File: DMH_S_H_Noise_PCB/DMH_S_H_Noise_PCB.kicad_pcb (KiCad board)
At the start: 2 copper layers, 48 x 120.8 mm, 82 parts, among them J0 Conn_01x01, J100 IDC_02x05, J200 IDC_02x05, J50 Conn_01x06, J60 Conn_01x06, J70 Conn_01x06, Q1 BC548, Q2 J113, Q3 BC548, SW1 SW_Push, SW2 SW_SPDT_321, U1 TL074, U2 TL074, U3 TL074

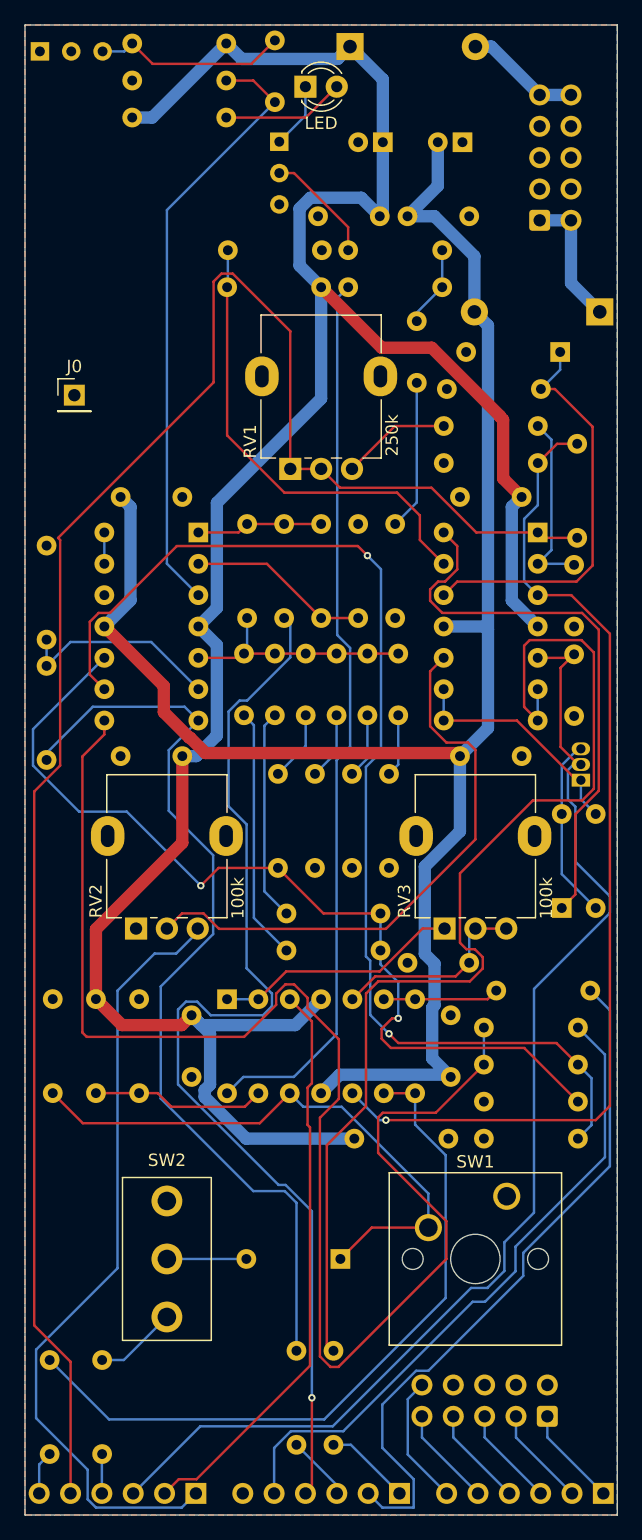
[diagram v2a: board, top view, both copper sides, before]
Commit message: Restarted positioning from scratch
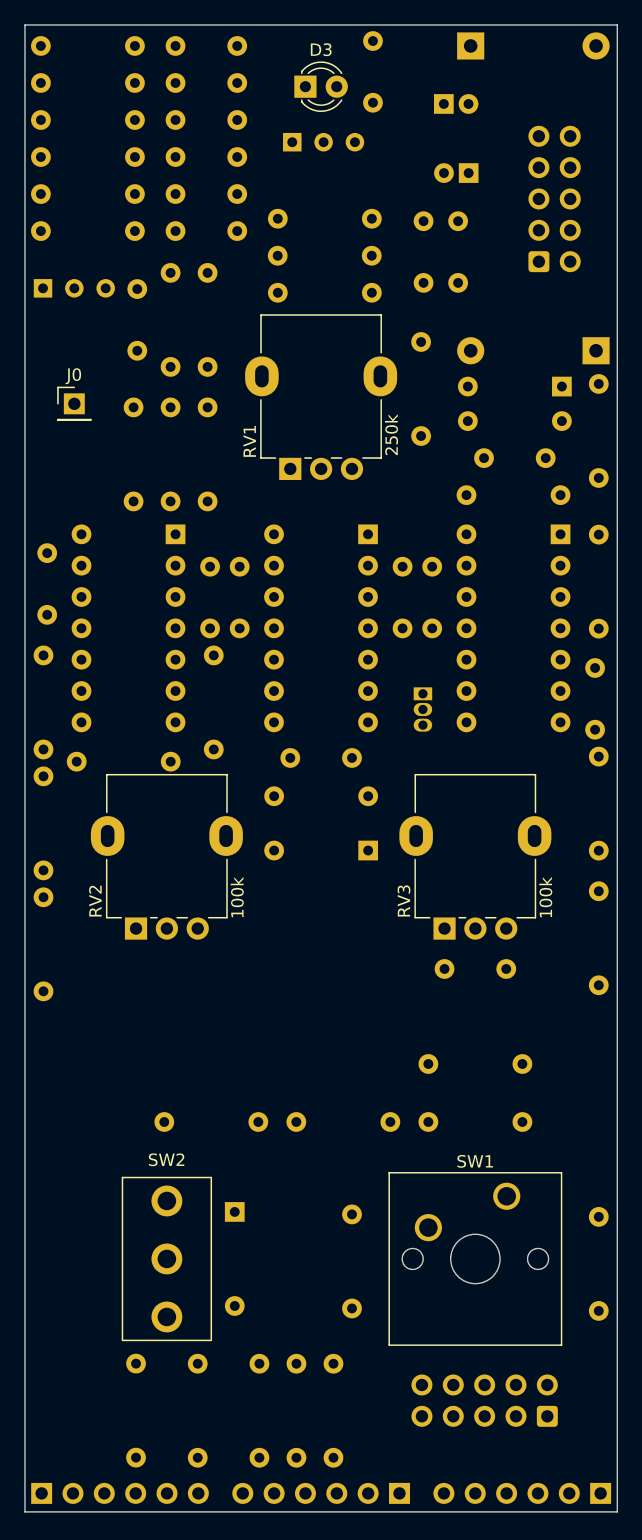
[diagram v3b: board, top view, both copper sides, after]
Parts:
- C10: value 1nF -> 100nF
- C11: value 100nF -> 2x1uF
- C12: value 1uF -> 1nF
- C13, C9: value 1uF -> 100nF
- C14: value 680pF -> 2x470nF
- C15: value 2.2nF -> 1uF
- C16: value 5.6nF -> 680pF
- C17: value 680pF -> 2.2nF
- C18: value 2.2nF -> 5.6nF
- C20: value 100nF -> 2.2nF
- C21: value 100nF -> 680pF
- D1: value LED -> SB140-; footprint LED_THT:LED_D3.0mm -> Diode_THT:D_DO-41_SOD81_P10.16mm_Horizontal; moved to B.Cu
- D2: value 1N4148 -> SB140+; footprint Diode_THT:D_DO-35_SOD27_P7.62mm_Horizontal -> Diode_THT:D_DO-41_SOD81_P10.16mm_Horizontal
- D3: value 1N4148 -> LED; footprint Diode_THT:D_DO-35_SOD27_P7.62mm_Horizontal -> LED_THT:LED_D3.0mm; moved to F.Cu
- D4: value SB140- -> 1N4148; footprint Diode_THT:D_DO-41_SOD81_P10.16mm_Horizontal -> Diode_THT:D_DO-35_SOD27_P7.62mm_Horizontal
- D5: value SB140+ -> 1N4148; footprint Diode_THT:D_DO-41_SOD81_P10.16mm_Horizontal -> Diode_THT:D_DO-35_SOD27_P7.62mm_Horizontal
- R1: value 100k -> 2x2k
- R11: value 1M -> 100k
- R12: value 1k -> 33k
- R13: value 1k -> 100k
- R14: value 100k -> 51k
- R15: value 100k -> 1M
- R16: value 270R -> 1k
- R17, R37: value 100k -> 1k
- R2, R6: value 2k -> 100k
- R20: value 4k7 -> 100k
- R21: value 47k -> 270R
- R22: value 470k -> 100k
- R23: value 22k -> 1k
- R25: value 1k -> 4k7
- R26: value 1M -> 47k
- R28: value 10k -> 22k
- R29: value 20k -> 100k
- R30: value 10k -> 1k
- R31: value 100K -> 1M
- R32: value 1k -> 470k
- R33: value 1k -> 10k
- R34: value 100k -> 20k
- R36: value 100k -> 100K
- R38: value 100k -> 2k
- R5: value 51k -> 100k
- R7: value 100k -> 10k
- R9: value 33k -> 100k
- moved R33 114.1 mm to (52.3, 44.2), turned to 0 degrees
- moved R25 105.2 mm to (59.9, 53.2), turned to 180 degrees
- moved R31 88.1 mm to (52.3, 50.2), turned to 0 degrees
- moved R32 88.1 mm to (52.3, 47.2), turned to 0 degrees
- moved R6 87.3 mm to (91.3, 131.4), turned to 180 degrees
- moved D4 78.7 mm to (68.0, 138.7), turned to -90 degrees
- moved D3 69.7 mm to (73.7, 47.5), turned to 0 degrees
- moved R23 69.3 mm to (73.0, 158.6)
- moved R18 68.4 mm to (65.0, 158.6)
- moved R5 67.4 mm to (91.3, 126.7), turned to 180 degrees
- moved R38 67.1 mm to (79.1, 58.2), turned to 180 degrees
- moved R26 64.4 mm to (59.9, 56.2)
- moved R17 63.6 mm to (77.5, 146.5), turned to 90 degrees
- moved R8 60.6 mm to (80.6, 131.4)
- moved C12 60.2 mm to (83.3, 58.4), turned to -90 degrees
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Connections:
- C10 pad 1: Net-(D2-A) -> GND
- C10 pad 2: Net-(C10-Pad2) -> -12V
- C11 pad 1: /Core Circuit/S&H -> GND
- C11 pad 2: GND -> Net-(U1A--)
- C12 pad 1: Net-(U2B-+) -> Net-(D5-A)
- C12 pad 2: GND -> Net-(C12-Pad2)
- C13 pad 1: Net-(Q3-E) -> /Core Circuit/S&H
- C13 pad 2: Net-(U3A-+) -> GND
- C14 pad 1: Net-(U3B-+) -> Net-(U2B-+)
- C14 pad 2: Net-(C14-Pad2) -> GND
- C15 pad 1: Net-(U3B-+) -> Net-(Q3-E)
- C15 pad 2: Net-(C15-Pad2) -> Net-(U3A-+)
- C20 pad 1: +12V -> Net-(U3B-+)
- C20 pad 2: GND -> Net-(C20-Pad2)
- C21 pad 1: GND -> Net-(U3B-+)
- C21 pad 2: -12V -> Net-(C21-Pad2)
- C9 pad 1: GND -> +12V
- C9 pad 2: Net-(U1A--) -> GND
- D1 pad 2: Net-(D1-A) -> -12V
- D2 pad 1: Net-(D2-K) -> +12V
- D4 pad 2: -12V -> Net-(D4-A)
- D5 pad 1: +12V -> Net-(D5-K)
- J100 pad 1a: Net-(D4-K) -> Net-(D1-K)
- J100 pad 1b: Net-(D4-K) -> Net-(D1-K)
- J100 pad 5a: Net-(D5-A) -> Net-(D2-A)
- J100 pad 5b: Net-(D5-A) -> Net-(D2-A)
- Q1 pad 1: Net-(D1-K) -> Net-(D3-K)
- Q2 pad 3: Net-(D3-A) -> Net-(D6-A)
- R1 pad 1: Net-(U1A-+) -> Net-(R1-Pad1)
- R1 pad 2: GND -> Net-(U1A--)
- R10 pad 1: +12V -> Net-(D5-A)
- R10 pad 2: Net-(U1D--) -> GND
- R11 pad 1: Net-(Q2-D) -> Net-(D5-K)
- R11 pad 2: Net-(D3-A) -> GND
- R12 pad 1: /Core Circuit/S&H Output -> Net-(U1D--)
- R12 pad 2: Net-(U1B--) -> GND
- R13 pad 1: /Core Circuit/Slew Output -> +12V
- R13 pad 2: Net-(U2B--) -> Net-(U1D--)
- R14 pad 1: +12V -> Net-(Q1-B)
- R14 pad 2: Net-(Q3-E) -> Net-(D5-A)
- R15 pad 1: Net-(U3A-+) -> Net-(Q2-D)
- R15 pad 2: GND -> Net-(D6-A)
- R16 pad 1: Net-(U3A--) -> /Core Circuit/S&H Output
- R16 pad 2: GND -> Net-(U1B--)
- R17 pad 1: Net-(R17-Pad1) -> /Core Circuit/Slew Output
- R17 pad 2: Net-(U3A--) -> Net-(U2B--)
- R18 pad 1: /Core Circuit/White -> /Core Circuit/Clock Output
- R18 pad 2: Net-(R17-Pad1) -> Net-(U2C--)
- R19 pad 1: Net-(U3B-+) -> +12V
- R19 pad 2: Net-(R17-Pad1) -> Net-(Q3-E)
- R2 pad 1: Net-(R2-Pad1) -> Net-(U1A-+)
- R2 pad 2: Net-(U1A--) -> GND
- R20 pad 1: Net-(C14-Pad2) -> Net-(U3A-+)
- R21 pad 1: Net-(C15-Pad2) -> Net-(U3A--)
- R22 pad 1: Net-(C16-Pad2) -> Net-(R22-Pad1)
- R22 pad 2: GND -> Net-(U3A--)
- R23 pad 1: Net-(U3B--) -> /Core Circuit/White
- R23 pad 2: GND -> Net-(R22-Pad1)
- R24 pad 1: Net-(U3B--) -> Net-(U3B-+)
- R24 pad 2: Net-(R24-Pad2) -> Net-(R22-Pad1)
- R25 pad 1: /Core Circuit/Pink -> Net-(C16-Pad2)
- R25 pad 2: Net-(R24-Pad2) -> GND
- R26 pad 1: Net-(U3C-+) -> Net-(C17-Pad2)
- R26 pad 2: Net-(C19-Pad2) -> GND
- R27 pad 1: Net-(U3C-+) -> Net-(C18-Pad2)
- R27 pad 2: Net-(C18-Pad2) -> GND
- R28 pad 1: Net-(U3C-+) -> Net-(U3B--)
- R28 pad 2: Net-(C17-Pad2) -> GND
- R29 pad 1: Net-(U3C-+) -> Net-(U3B--)
- R29 pad 2: GND -> Net-(R29-Pad2)
- R30 pad 1: Net-(U3C--) -> /Core Circuit/Pink
- R30 pad 2: GND -> Net-(R29-Pad2)
- R31 pad 1: Net-(U3C--) -> Net-(U3C-+)
- R31 pad 2: Net-(R31-Pad2) -> Net-(C19-Pad2)
- R32 pad 1: /Core Circuit/Blue -> Net-(U3C-+)
- R32 pad 2: Net-(R31-Pad2) -> Net-(C20-Pad2)
- R33 pad 1: /Core Circuit/Clock Output -> Net-(U3C-+)
- R33 pad 2: Net-(U2C--) -> Net-(C21-Pad2)
- R34 pad 1: GND -> Net-(U3C-+)
- R34 pad 2: Net-(D6-K) -> GND
- R35 pad 1: Net-(U2D--) -> Net-(U3C--)
- R36 pad 1: Net-(R36-Pad1) -> Net-(U3C--)
- R36 pad 2: Net-(C10-Pad2) -> Net-(R36-Pad2)
- R37 pad 1: Net-(R37-Pad1) -> /Core Circuit/Blue
- R37 pad 2: +12V -> Net-(R36-Pad2)
- R38 pad 2: Net-(U2D--) -> Net-(D3-A)
- R5 pad 1: Net-(Q1-B) -> GND
- R5 pad 2: Net-(C10-Pad2) -> Net-(D4-K)
- R6 pad 1: +12V -> Net-(R6-Pad1)
- R6 pad 2: Net-(D1-A) -> +12V
- R7 pad 1: Net-(D2-A) -> Net-(U2D--)
- R8 pad 1: Net-(D2-K) -> +12V
- R8 pad 2: GND -> Net-(U2D--)
- R9 pad 1: Net-(U1D--) -> Net-(R9-Pad1)
- R9 pad 2: GND -> Net-(C12-Pad2)
- RV1 pad 3: Net-(R2-Pad1) -> Net-(R1-Pad1)
- SW1 pad 1: Net-(R37-Pad1) -> Net-(R6-Pad1)
- SW1 pad 2: Net-(D6-K) -> Net-(D4-K)
- SW2 pad 2: Net-(D6-A) -> Net-(D4-A)
- U1 pad 12: Net-(D2-K) -> Net-(D5-K)
- U1 pad 14: Net-(D3-K) -> Net-(D6-K)
- U2 pad 12: Net-(D6-K) -> Net-(D4-K)
- U2 pad 14: Net-(R36-Pad1) -> Net-(R9-Pad1)
- U3 pad 1: Net-(R17-Pad1) -> Net-(R22-Pad1)
- U3 pad 7: Net-(R24-Pad2) -> Net-(R29-Pad2)
- U3 pad 8: Net-(R31-Pad2) -> Net-(R36-Pad2)
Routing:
- net +12V: track 197.2 -> 0.00 mm
- net /Core Circuit/Internal Clock: track 150.7 -> 0.00 mm
- net -12V: track 144.9 -> 0.00 mm
- net Net-(R31-Pad2): track 119.2 -> 0.00 mm
- net /Core Circuit/S&H: track 97.6 -> 0.00 mm
- net Net-(U3C--): track 95.1 -> 0.00 mm, vias 2 -> 0
- net Net-(U1B--): track 89.7 -> 0.00 mm
- net /Core Circuit/White: track 88.4 -> 0.00 mm, vias 1 -> 0
- net Net-(U1A-+): track 83.1 -> 0.00 mm, vias 1 -> 0
- net Net-(R24-Pad2): track 76.2 -> 0.00 mm
- net Net-(U3C-+): track 75.1 -> 0.00 mm, vias 2 -> 0
- net Net-(R36-Pad1): track 72.7 -> 0.00 mm
- net /Core Circuit/Input: track 64.0 -> 0.00 mm
- net Net-(U2C--): track 58.7 -> 0.00 mm
- net /Core Circuit/Slew Output: track 56.0 -> 0.00 mm
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- removed copper zone on B.Cu, net GND
- removed copper zone on F.Cu, net GND
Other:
- board size 48 x 120.8 mm -> 48 x 120.5 mm

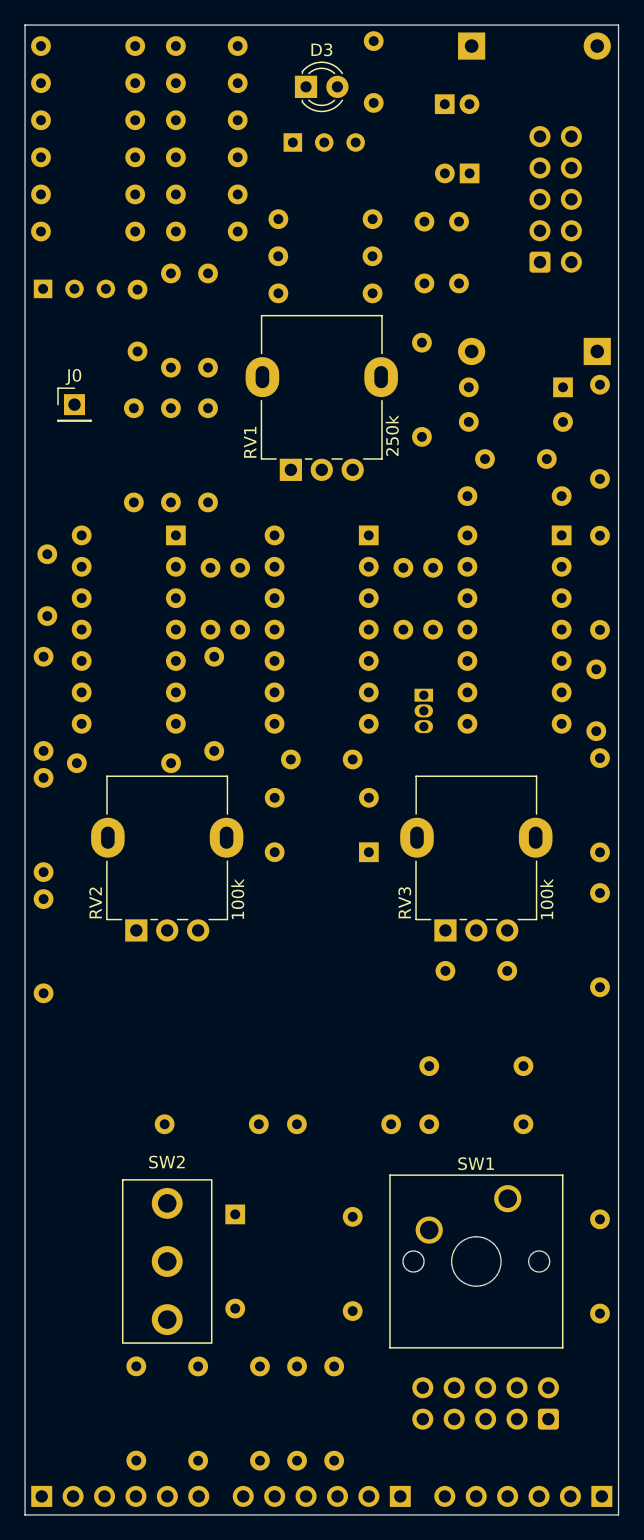
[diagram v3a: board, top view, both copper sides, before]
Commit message: Minor positioning corrections
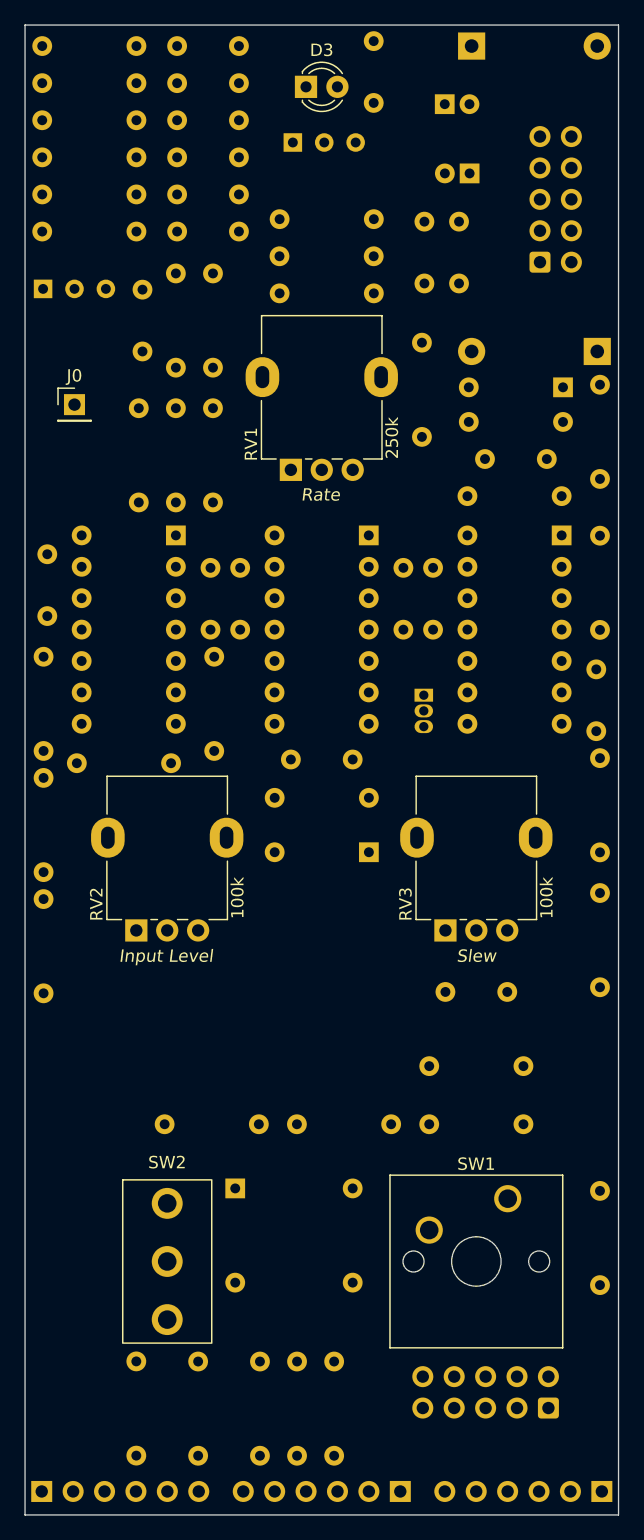
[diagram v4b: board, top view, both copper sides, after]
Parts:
- RV1, RV2, RV3: footprint Potentiometer_THT:Potentiometer_Alpha_RD901F-40-00D_Single_Vertical -> SynthStuff:Potentiometer_Alpha_RD901F-40-00D_Single_Vertical
- SW1: footprint Button_Switch_Keyboard:SW_Cherry_MX_1.00u_PCB -> SynthStuff:SW_Cherry_MX_1.00u_PCB
- moved R16 2.30 mm to (97.5, 144.4)
- moved R17 2.30 mm to (77.5, 144.2)
- moved D4 2.10 mm to (68.0, 136.6)
- moved C14 1.70 mm to (85.0, 120.7)
- moved J200 0.90 mm to (93.3, 154.4)
- moved J50 0.40 mm to (52.4, 161.1)
- moved J60 0.40 mm to (81.3, 161.1)
- moved J70 0.40 mm to (97.7, 161.1)
- moved R18 0.40 mm to (65.0, 158.2)
- moved R19 0.40 mm to (63.2, 70.2)
- moved R20 0.40 mm to (66.2, 70.2)
- moved R21 0.40 mm to (60.2, 81.1)
- moved R22 0.40 mm to (66.2, 73.5)
- moved R23 0.40 mm to (73.0, 158.2)
- moved R24 0.40 mm to (63.2, 73.5)
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
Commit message: Rerouting finished
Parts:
- moved C10 9.50 mm to (52.6, 75.8), turned to 0 degrees
- moved R2 7.64 mm to (97.5, 79.2), turned to 90 degrees
- moved R34 5.11 mm to (52.5, 88.5), turned to 90 degrees
- moved C5 4.70 mm to (93.1, 101.9), turned to 180 degrees
- moved R35 3.85 mm to (54.1, 116.7)
- moved R36 3.85 mm to (54.1, 114.5)
- moved C7 2.57 mm to (81.6, 89.0)
- moved R1 1.89 mm to (84.9, 80.6)
- moved C13 1.80 mm to (75.7, 101.9)
- moved C1 0.80 mm to (84.1, 48.9)
- moved C2 0.80 mm to (86.2, 54.5)
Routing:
- net +12V: track 0.00 -> 211.8 mm
- net /Core Circuit/Internal Clock: track 0.00 -> 121.0 mm
- net -12V: track 0.00 -> 118.6 mm
- net /Core Circuit/S&H: track 0.00 -> 100.3 mm
- net /Core Circuit/Input: track 0.00 -> 95.1 mm
- net /Core Circuit/Slew Input: track 0.00 -> 85.0 mm
- net Net-(R22-Pad1): track 0.00 -> 82.4 mm
- net Net-(D4-K): track 0.00 -> 81.0 mm
- net Net-(U2B--): track 0.00 -> 78.7 mm
- net Net-(U2A--): track 0.00 -> 76.9 mm
- net Net-(U2B-+): track 0.00 -> 76.1 mm
- net Net-(U3B-+): track 0.00 -> 68.2 mm
- net Net-(R29-Pad2): track 0.00 -> 61.2 mm
- net Net-(R36-Pad2): track 0.00 -> 58.9 mm
- net Net-(U2C--): track 0.00 -> 58.7 mm
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- added copper zone on B.Cu, net GND
- added copper zone on F.Cu, net GND

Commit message: Minor corrections
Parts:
- R38: value 2k -> 100R
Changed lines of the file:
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@@
 		)
 		(property "Value" "250k"
-			(at 2.575 8.2 -90)
+			(at 2.575 8.25 -90)
 			(layer "F.SilkS")
 			(effects
@@
 				(font
 					(size 1 1)
-					(thickness 0.1)
+					(thickness 0.15)
 					(italic yes)
 				)
@@
 		)
 		(property "Value" "100k"
-			(at 2.625 8.2 -90)
+			(at 2.625 8.25 -90)
 			(layer "F.SilkS")
 			(effects
@@
 				(font
 					(size 1 1)
-					(thickness 0.1)
+					(thickness 0.15)
 					(italic yes)
 				)
@@
 		)
 		(property "Value" "100k"
-			(at 2.625 8.2 -90)
+			(at 2.625 8.25 -90)
 			(layer "F.SilkS")
 			(effects
@@
 				(font
 					(size 1 1)
-					(thickness 0.1)
+					(thickness 0.15)
 					(italic yes)
 				)
@@
 		)
 		(property "Value" "100nF"
-			(at 2.5 0 90)
+			(at 3.1 0 90)
 			(layer "B.SilkS")
 			(effects
@@
 	)
 	(footprint "Connector_PinHeader_2.54mm:PinHeader_1x06_P2.54mm_Vertical"
+		(locked yes)
 		(layer "B.Cu")
 		(at 52.35 161.1 -90)
@@
 		(tags "Resistor Axial_DIN0207 series Axial Horizontal pin pitch 7.62mm 0.25W = 1/4W length 6.3mm diameter 2.5mm")
 		(property "Reference" "R34"
-			(at -1.665 0.025 360)
+			(at -1.665 0.025 0)
 			(layer "B.SilkS")
 			(effects
@@
 		(tags "Resistor Axial_DIN0207 series Axial Horizontal pin pitch 7.62mm 0.25W = 1/4W length 6.3mm diameter 2.5mm")
 		(property "Reference" "R19"
-			(at 9.11 0 180)
+			(at 8.96 0 180)
 			(layer "B.SilkS")
 			(effects
@@
 		)
 		(property "Value" "100nF"
-			(at 2.5 0 360)
+			(at 1.9 0 0)
 			(layer "B.SilkS")
 			(effects
@@
 		)
 		(fp_text user "${REFERENCE}"
-			(at 2.5 0 360)
+			(at 2.5 0 0)
 			(layer "B.Fab")
 			(effects
@@
 		)
 		(property "Value" "100nF"
-			(at 2.5 0 0)
+			(at 3.2 0 0)
 			(layer "B.SilkS")
 			(effects
@@
 		)
 		(property "Value" "100nF"
-			(at 2.5 0 90)
+			(at 3.025 0 90)
 			(layer "B.SilkS")
 			(effects
@@
 		(tags "TO-92L Inline Wide transistor")
 		(property "Reference" "Q2"
-			(at -2.3 -0.05 180)
+			(at 4.8 -0.05 180)
 			(layer "B.SilkS")
 			(effects
@@
 		(tags "Resistor Axial_DIN0207 series Axial Horizontal pin pitch 7.62mm 0.25W = 1/4W length 6.3mm diameter 2.5mm")
 		(property "Reference" "R2"
-			(at 9.31 -0.5 360)
+			(at -1.515 0 0)
 			(layer "B.SilkS")
 			(effects
@@
 		(tags "Resistor Axial_DIN0207 series Axial Horizontal pin pitch 7.62mm 0.25W = 1/4W length 6.3mm diameter 2.5mm")
 		(property "Reference" "R36"
-			(at 3.81 2.37 90)
+			(at 3.26 2.37 90)
 			(layer "B.SilkS")
 			(effects
@@
 			)
 		)
-		(property "Value" "2k"
+		(property "Value" "100R"
 			(at 3.81 0 0)
 			(layer "B.SilkS")
@@
 		(sheetname "Core Circuit")
 		(sheetfile "Core_Circuit.kicad_sch")
-		(attr through_hole dnp)
+		(attr through_hole)
 		(fp_line
 			(start 7.08 1.37)
@@
 	)
 	(footprint "Connector_PinHeader_2.54mm:PinHeader_1x06_P2.54mm_Vertical"
+		(locked yes)
 		(layer "B.Cu")
 		(at 81.35 161.1 90)
@@
 		)
 		(property "Value" "100nF"
-			(at 2.5 0 90)
+			(at 3.1 0 90)
 			(layer "B.SilkS")
 			(effects
@@
 	(footprint "Resistor_THT:R_Axial_DIN0207_L6.3mm_D2.5mm_P7.62mm_Horizontal"
 		(layer "B.Cu")
-		(at 65 158.21 90)
+		(at 65 158.185 90)
 		(descr "Resistor, Axial_DIN0207 series, Axial, Horizontal, pin pitch=7.62mm, 0.25W = 1/4W, length*diameter=6.3*2.5mm^2, http://cdn-reichelt.de/documents/datenblatt/B400/1_4W%23YAG.pdf")
 		(tags "Resistor Axial_DIN0207 series Axial Horizontal pin pitch 7.62mm 0.25W = 1/4W length 6.3mm diameter 2.5mm")
@@
 		)
 		(property "Value" "100nF"
-			(at 2.5 0 90)
+			(at 3.1 0 90)
 			(layer "B.SilkS")
 			(effects
@@
 		)
 		(property "Value" "100nF"
-			(at 2.5 0 90)
+			(at 1.9 0 90)
 			(layer "B.SilkS")
 			(effects
@@
 		(tags "Resistor Axial_DIN0207 series Axial Horizontal pin pitch 7.62mm 0.25W = 1/4W length 6.3mm diameter 2.5mm")
 		(property "Reference" "R20"
-			(at 9.11 0 180)
+			(at 8.96 0 180)
 			(layer "B.SilkS")
 			(effects
@@
 	)
 	(footprint "Connector_PinHeader_2.54mm:PinHeader_1x06_P2.54mm_Vertical"
+		(locked yes)
 		(layer "B.Cu")
 		(at 97.65 161.1 90)
@@
 		)
 		(property "Value" "100nF"
-			(at 2.5 0 360)
+			(at 3.1 0 0)
 			(layer "B.SilkS")
 			(effects
@@
 		)
 		(fp_text user "${REFERENCE}"
-			(at 2.5 0 360)
+			(at 2.5 0 0)
 			(layer "B.Fab")
 			(effects
@@
 	)
 	(segment
-		(start 62.51 159.144365)
-		(end 69.254365 152.4)
-		(width 0.2)
-		(layer "B.Cu")
-		(net 29)
-	)
-	(segment
-		(start 77.1 146.9)
-		(end 74.5 144.3)
+		(start 75.8 152.4)
+		(end 77.1 151.1)
 		(width 0.2)
 		(layer "B.Cu")
@@
 	)
 	(segment
-		(start 69.254365 152.4)
+		(start 68.5 152.4)
 		(end 75.8 152.4)
 		(width 0.2)
@@
 	)
 	(segment
-		(start 75.8 152.4)
-		(end 77.1 151.1)
+		(start 62.51 158.39)
+		(end 68.5 152.4)
 		(width 0.2)
 		(layer "B.Cu")
@@
 	(segment
 		(start 62.51 161.1)
-		(end 62.51 159.144365)
+		(end 62.51 158.39)
 		(width 0.2)
 		(layer "B.Cu")
@@
 		(width 0.2)
 		(layer "B.Cu")
+		(net 29)
+	)
+	(segment
+		(start 77.1 146.9)
+		(end 74.5 144.3)
+		(width 0.2)
+		(layer "B.Cu")
